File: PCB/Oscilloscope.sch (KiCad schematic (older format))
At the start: 21 parts

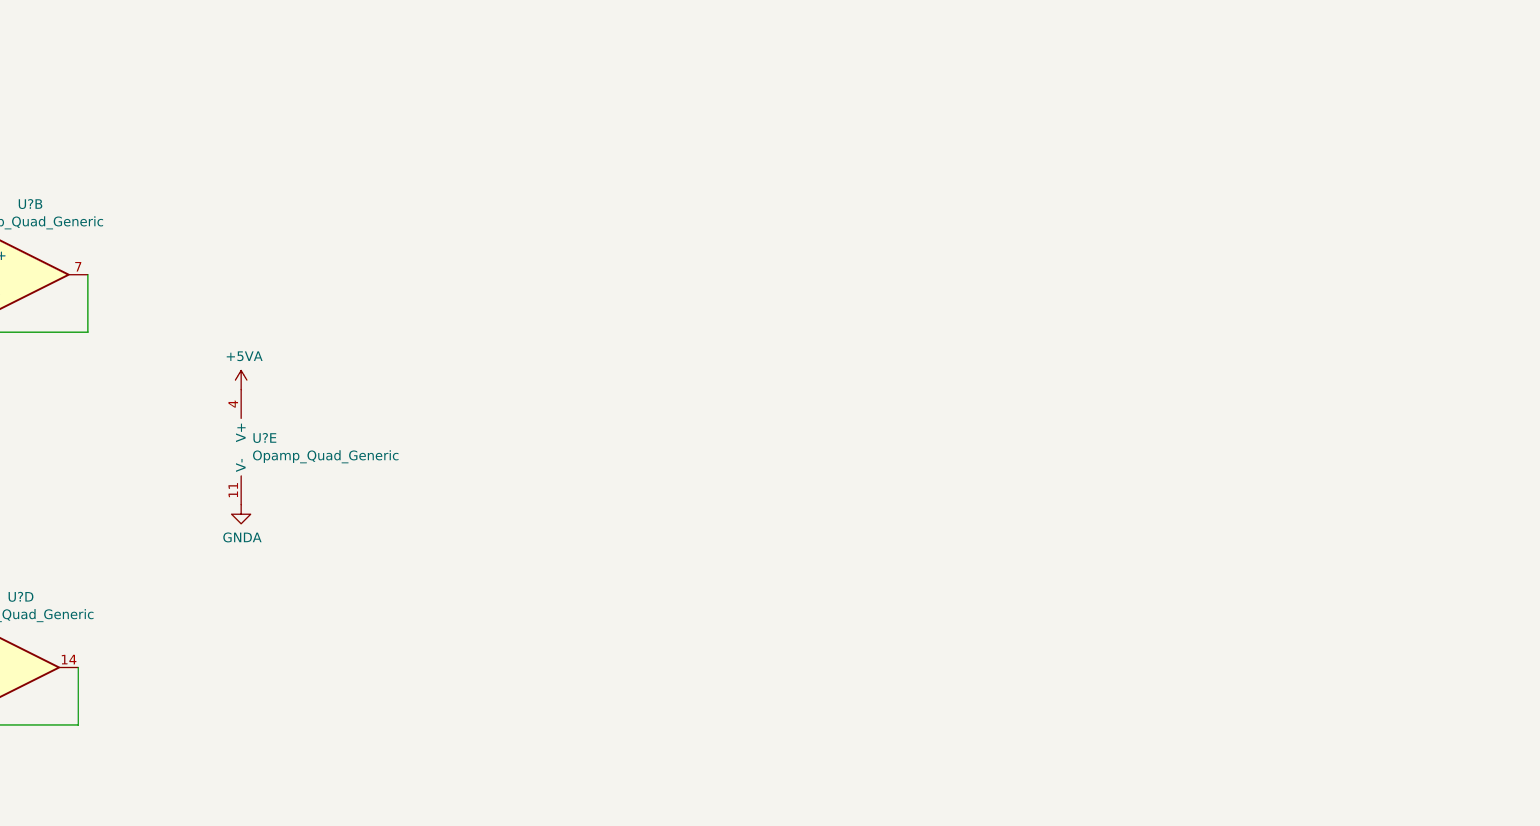
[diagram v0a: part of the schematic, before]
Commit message: Added USB footprint and modified schematic
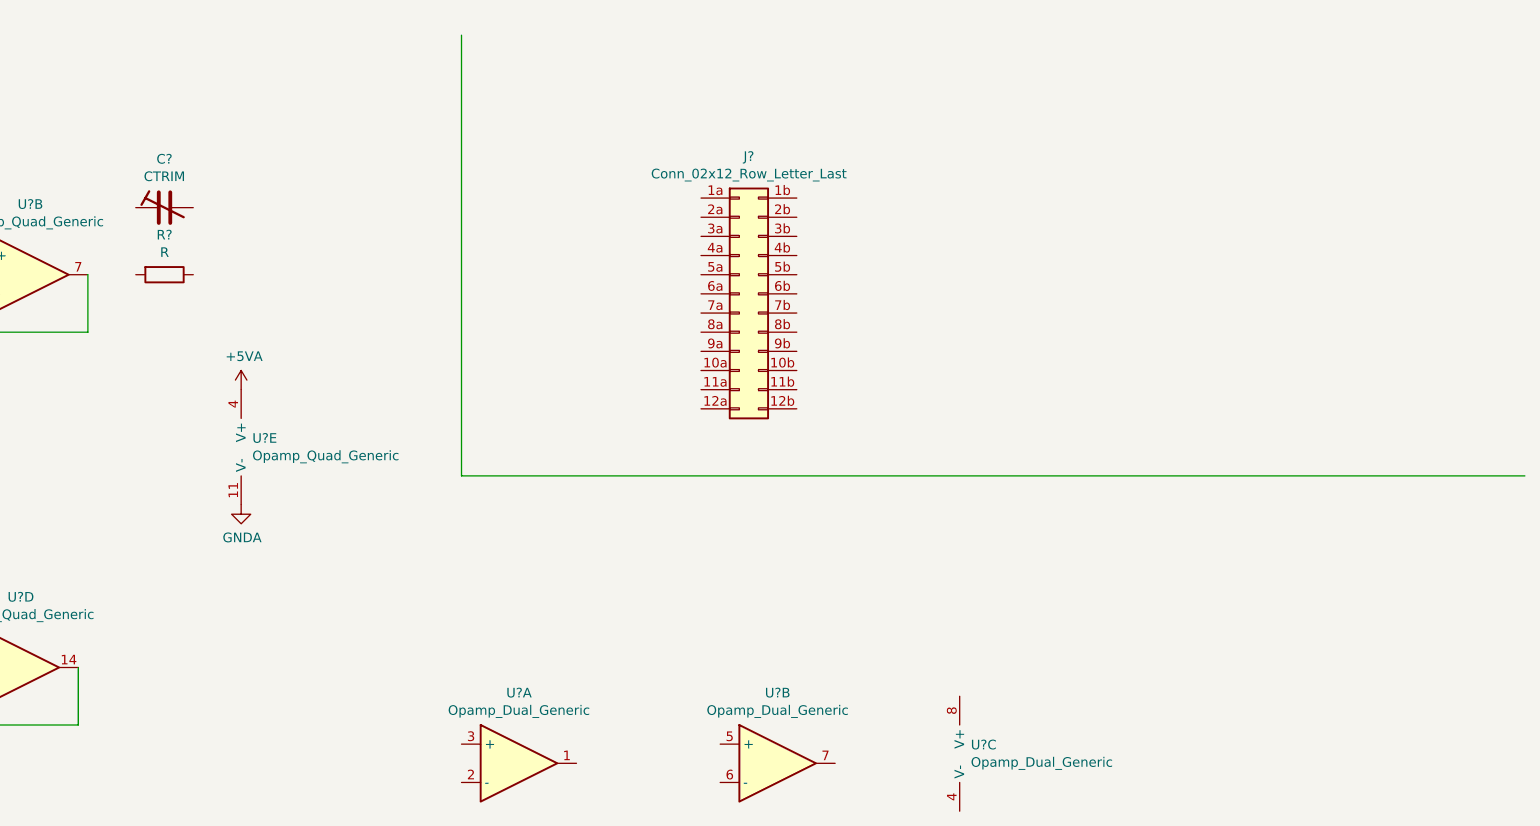
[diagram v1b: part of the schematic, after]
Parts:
- added C?: CTRIM, symbol Device:CTRIM
- added J?: Conn_02x12_Row_Letter_Last, symbol Connector_Generic:Conn_02x12_Row_Letter_Last
- added R?: R, symbol Device:R
- added U? (x3): Opamp_Dual_Generic, symbol Device:Opamp_Dual_Generic
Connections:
- wire segments 44 -> 46
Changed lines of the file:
@@
 $Descr A4 11693 8268
 encoding utf-8
-Sheet 2 5
+Sheet 2 3
 Title ""
 Date ""
@@
 	2850 3900 3000 3900
 $Comp
-L power:GNDA #PWR?
+L power:GNDA #PWR0117
 U 1 1 5E8B3DC5
 P 2550 4050
-F 0 "#PWR?" H 2550 3800 50  0001 C CNN
+F 0 "#PWR0117" H 2550 3800 50  0001 C CNN
 F 1 "GNDA" H 2555 3877 50  0000 C CNN
 F 2 "" H 2550 4050 50  0001 C CNN
@@
 $EndComp
 $Comp
-L power:GNDA #PWR?
+L power:GNDA #PWR0118
 U 1 1 5E8B4AEE
 P 1100 4200
-F 0 "#PWR?" H 1100 3950 50  0001 C CNN
+F 0 "#PWR0118" H 1100 3950 50  0001 C CNN
 F 1 "GNDA" H 1105 4027 50  0000 C CNN
 F 2 "" H 1100 4200 50  0001 C CNN
@@
 $EndComp
 $Comp
-L power:GNDA #PWR?
+L power:GNDA #PWR0119
 U 1 1 5E8B4E02
 P 2850 2150
-F 0 "#PWR?" H 2850 1900 50  0001 C CNN
+F 0 "#PWR0119" H 2850 1900 50  0001 C CNN
 F 1 "GNDA" H 2855 1977 50  0000 C CNN
 F 2 "" H 2850 2150 50  0001 C CNN
@@
 $EndComp
 $Comp
-L power:GNDA #PWR?
+L power:GNDA #PWR0120
 U 1 1 5E8B5E64
 P 850 2000
-F 0 "#PWR?" H 850 1750 50  0001 C CNN
+F 0 "#PWR0120" H 850 1750 50  0001 C CNN
 F 1 "GNDA" H 855 1827 50  0000 C CNN
 F 2 "" H 850 2000 50  0001 C CNN
@@
 	1100 1650 1350 1650
 $Comp
-L power:GNDA #PWR?
+L power:GNDA #PWR0121
 U 1 1 5E8EE81D
 P 2550 2000
-F 0 "#PWR?" H 2550 1750 50  0001 C CNN
+F 0 "#PWR0121" H 2550 1750 50  0001 C CNN
 F 1 "GNDA" H 2555 1827 50  0000 C CNN
 F 2 "" H 2550 2000 50  0001 C CNN
@@
 $EndComp
 $Comp
-L power:GNDA #PWR?
+L power:GNDA #PWR0122
 U 1 1 5E8F1CAA
 P 1100 2150
-F 0 "#PWR?" H 1100 1900 50  0001 C CNN
+F 0 "#PWR0122" H 1100 1900 50  0001 C CNN
 F 1 "GNDA" H 1105 1977 50  0000 C CNN
 F 2 "" H 1100 2150 50  0001 C CNN
@@
 $EndComp
 $Comp
-L power:GNDA #PWR?
+L power:GNDA #PWR0123
 U 1 1 5E8F2DB9
 P 850 4050
-F 0 "#PWR?" H 850 3800 50  0001 C CNN
+F 0 "#PWR0123" H 850 3800 50  0001 C CNN
 F 1 "GNDA" H 855 3877 50  0000 C CNN
 F 2 "" H 850 4050 50  0001 C CNN
@@
 $EndComp
 $Comp
-L power:GNDA #PWR?
+L power:GNDA #PWR0124
 U 1 1 5E8F4144
 P 2850 4200
-F 0 "#PWR?" H 2850 3950 50  0001 C CNN
+F 0 "#PWR0124" H 2850 3950 50  0001 C CNN
 F 1 "GNDA" H 2855 4027 50  0000 C CNN
 F 2 "" H 2850 4200 50  0001 C CNN
@@
 $EndComp
 $Comp
-L power:+5VA #PWR?
+L power:+5VA #PWR0125
 U 1 1 5E907F1D
 P 4500 2350
-F 0 "#PWR?" H 4500 2200 50  0001 C CNN
+F 0 "#PWR0125" H 4500 2200 50  0001 C CNN
 F 1 "+5VA" H 4515 2523 50  0000 C CNN
 F 2 "" H 4500 2350 50  0001 C CNN
@@
 $EndComp
 $Comp
-L power:+5VA #PWR?
+L power:+5VA #PWR0126
 U 1 1 5E9083AD
 P 1100 1300
-F 0 "#PWR?" H 1100 1150 50  0001 C CNN
+F 0 "#PWR0126" H 1100 1150 50  0001 C CNN
 F 1 "+5VA" H 1115 1473 50  0000 C CNN
 F 2 "" H 1100 1300 50  0001 C CNN
@@
 $EndComp
 $Comp
-L power:+5VA #PWR?
+L power:+5VA #PWR0127
 U 1 1 5E90B4C3
 P 2800 1300
-F 0 "#PWR?" H 2800 1150 50  0001 C CNN
+F 0 "#PWR0127" H 2800 1150 50  0001 C CNN
 F 1 "+5VA" H 2815 1473 50  0000 C CNN
 F 2 "" H 2800 1300 50  0001 C CNN
@@
 $EndComp
 $Comp
-L power:+5VA #PWR?
+L power:+5VA #PWR0128
 U 1 1 5E90BBBE
 P 1100 3350
-F 0 "#PWR?" H 1100 3200 50  0001 C CNN
+F 0 "#PWR0128" H 1100 3200 50  0001 C CNN
 F 1 "+5VA" H 1115 3523 50  0000 C CNN
 F 2 "" H 1100 3350 50  0001 C CNN
@@
 $EndComp
 $Comp
-L power:+5VA #PWR?
+L power:+5VA #PWR0129
 U 1 1 5E90CE52
 P 2800 3350
-F 0 "#PWR?" H 2800 3200 50  0001 C CNN
+F 0 "#PWR0129" H 2800 3200 50  0001 C CNN
 F 1 "+5VA" H 2815 3523 50  0000 C CNN
 F 2 "" H 2800 3350 50  0001 C CNN
@@
 $EndComp
 $Comp
-L power:GNDA #PWR?
+L power:GNDA #PWR0130
 U 1 1 5E90F47D
 P 4500 2950
-F 0 "#PWR?" H 4500 2700 50  0001 C CNN
+F 0 "#PWR0130" H 4500 2700 50  0001 C CNN
 F 1 "GNDA" H 4505 2777 50  0000 C CNN
 F 2 "" H 4500 2950 50  0001 C CNN
@@
 Text GLabel 2550 3250 1    50   Input ~ 0
 analog_input_1
+$Comp
+L Connector_Generic:Conn_02x12_Row_Letter_Last J?
+U 1 1 5E8BD1E2
+P 7100 1850
+F 0 "J?" H 7150 2567 50  0000 C CNN
+F 1 "Conn_02x12_Row_Letter_Last" H 7150 2476 50  0000 C CNN
+F 2 "" H 7100 1850 50  0001 C CNN
+F 3 "~" H 7100 1850 50  0001 C CNN
+	1    7100 1850
+	1    0    0    -1
+$EndComp
+$Comp
+L Device:Opamp_Dual_Generic U?
+U 1 1 5E8C2412
+P 5950 4300
+AR Path="/5E84F5D5/5E8C2412" Ref="U?"  Part="1"
+AR Path="/5E84F4C6/5E8C2412" Ref="U?"  Part="1"
+F 0 "U?" H 5950 4667 50  0000 C CNN
+F 1 "Opamp_Dual_Generic" H 5950 4576 50  0000 C CNN
+F 2 "" H 5950 4300 50  0001 C CNN
+F 3 "~" H 5950 4300 50  0001 C CNN
+	1    5950 4300
+	1    0    0    -1
+$EndComp
+$Comp
+L Device:Opamp_Dual_Generic U?
+U 2 1 5E8C2418
+P 7300 4300
+AR Path="/5E84F5D5/5E8C2418" Ref="U?"  Part="2"
+AR Path="/5E84F4C6/5E8C2418" Ref="U?"  Part="2"
+F 0 "U?" H 7300 4667 50  0000 C CNN
+F 1 "Opamp_Dual_Generic" H 7300 4576 50  0000 C CNN
+F 2 "" H 7300 4300 50  0001 C CNN
+F 3 "~" H 7300 4300 50  0001 C CNN
+	2    7300 4300
+	1    0    0    -1
+$EndComp
+$Comp
+L Device:Opamp_Dual_Generic U?
+U 3 1 5E8C241E
+P 8350 4250
+AR Path="/5E84F5D5/5E8C241E" Ref="U?"  Part="3"
+AR Path="/5E84F4C6/5E8C241E" Ref="U?"  Part="3"
+F 0 "U?" H 8308 4296 50  0000 L CNN
+F 1 "Opamp_Dual_Generic" H 8308 4205 50  0000 L CNN
+F 2 "" H 8350 4250 50  0001 C CNN
+F 3 "~" H 8350 4250 50  0001 C CNN
+	3    8350 4250
+	1    0    0    -1
+$EndComp
+$Comp
+L Device:R R?
+U 1 1 5E90D0F4
+P 4100 1750
+F 0 "R?" V 3893 1750 50  0000 C CNN
+F 1 "R" V 3984 1750 50  0000 C CNN
+F 2 "" V 4030 1750 50  0001 C CNN
+F 3 "~" H 4100 1750 50  0001 C CNN
+	1    4100 1750
+	0    1    1    0
+$EndComp
+$Comp
+L Device:CTRIM C?
+U 1 1 5E90E27B
+P 4100 1400
+F 0 "C?" V 4353 1400 50  0000 C CNN
+F 1 "CTRIM" V 4262 1400 50  0000 C CNN
+F 2 "" H 4100 1400 50  0001 C CNN
+F 3 "~" H 4100 1400 50  0001 C CNN
+	1    4100 1400
+	0    -1   -1   0
+$EndComp
+Wire Wire Line
+	11200 2800 5650 2800
+Wire Wire Line
+	5650 2800 5650 500
 $EndSCHEMATC

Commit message: Advancing in the schmatic. Power to be finished
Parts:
- removed C?: CTRIM, symbol Device:CTRIM
- removed R?: R, symbol Device:R
- added D? (x4): D_Zener, symbol Device:D_Zener
- added R? (x9): R, symbol Device:R
- added R? (x23): 100R, symbol Device:R
- added U? (x5): LM2901, symbol Comparator:LM2901
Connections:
- net labels added: analog_output_1, analog_output_2, analon_input_1, analon_input_2, analon_input_3, analon_input_4, digital_input_1, digital_input_10, digital_input_11, digital_input_12, digital_input_13, digital_input_14, digital_input_15, digital_input_16, digital_input_17, digital_input_18, digital_input_19, digital_input_2, digital_input_20, digital_input_21, digital_input_22, digital_input_23, digital_input_24, digital_input_3, digital_input_4, digital_input_5, digital_input_6, digital_input_7, digital_input_8, digital_input_9, trigger_1, trigger_2, trigger_3, trigger_4
- net labels removed: analog_input_1
- wire segments 46 -> 74
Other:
- moved on the sheet: J?, R?, U?A, U?B, U?C, U?D, U?E

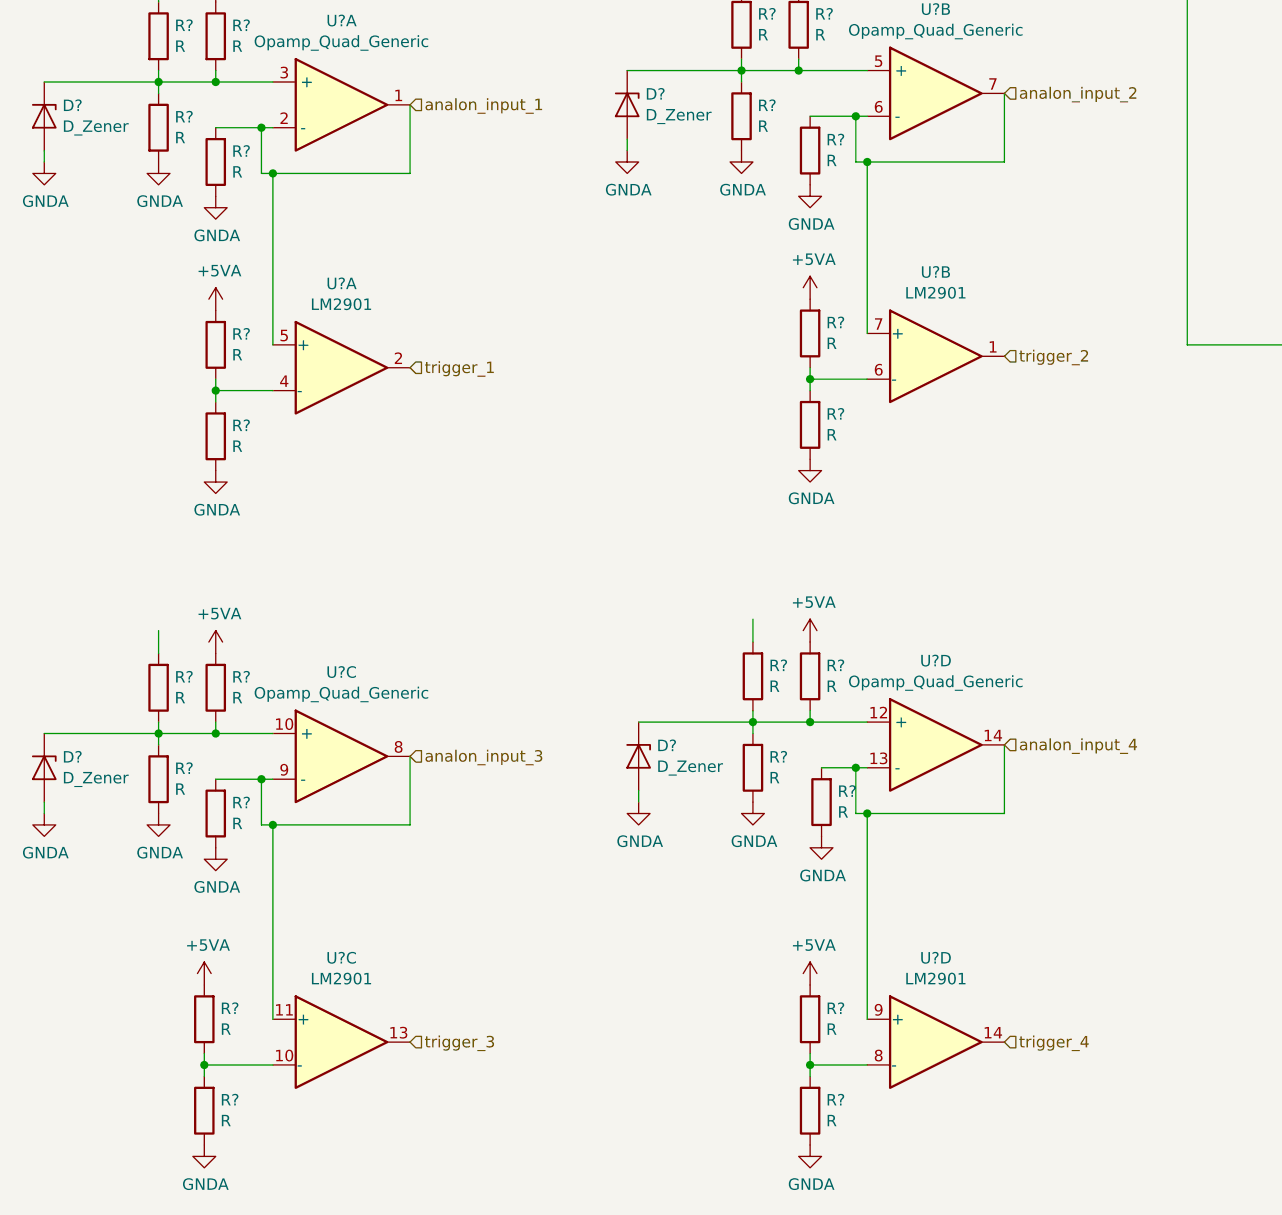
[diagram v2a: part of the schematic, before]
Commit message: Changed microcontroller, schemtic modified
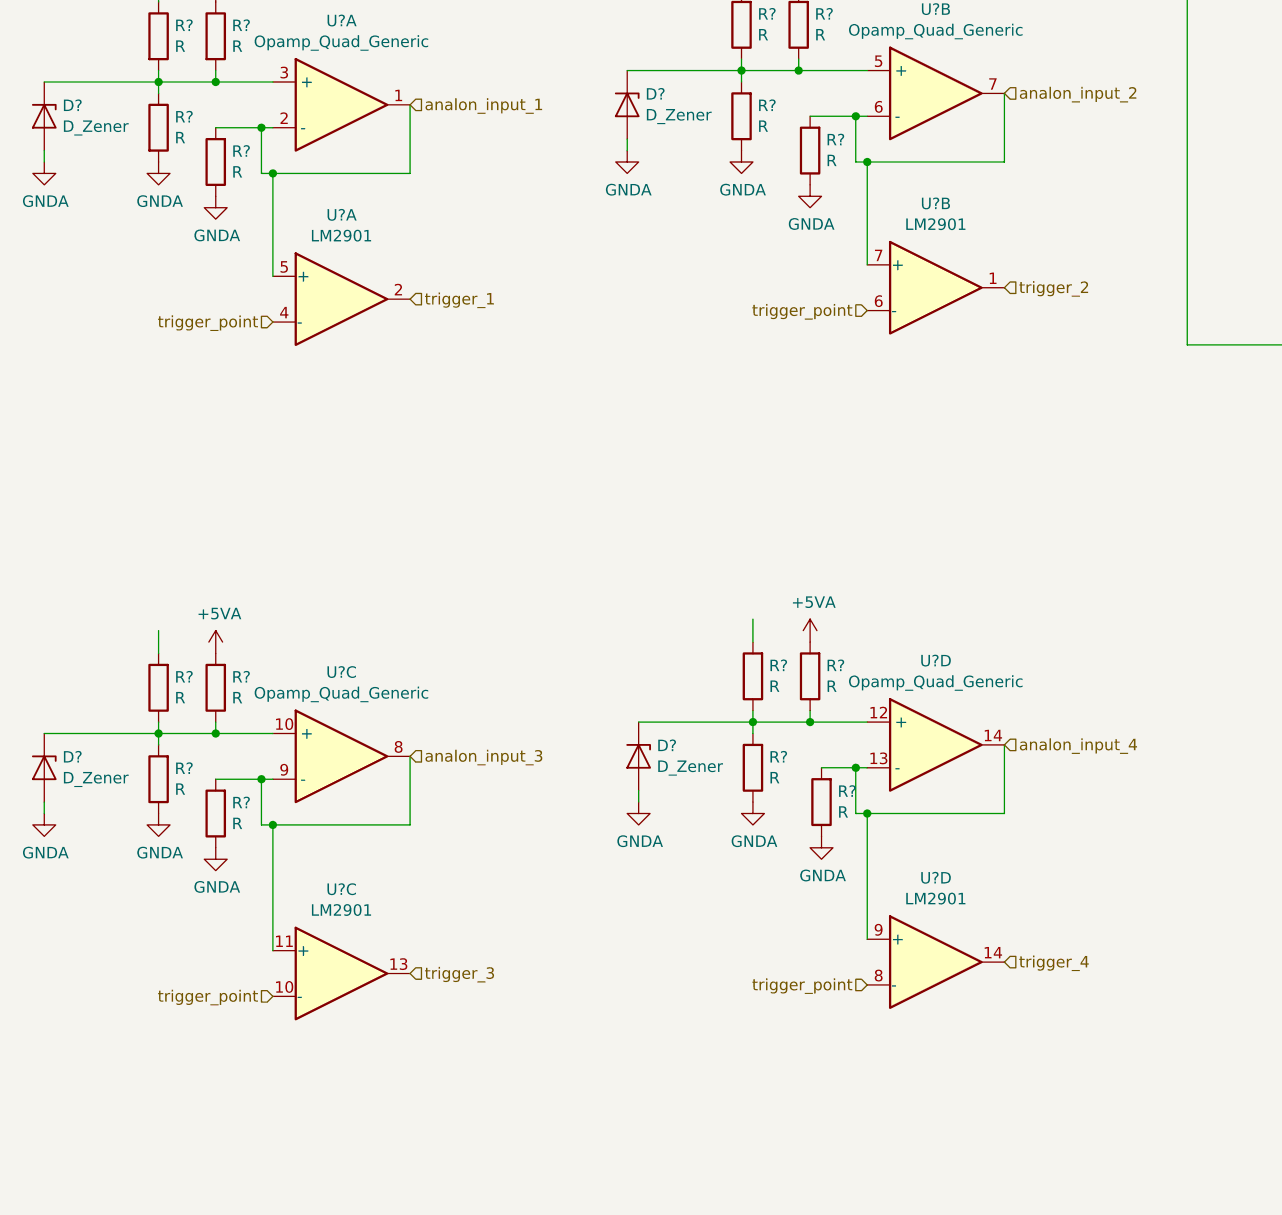
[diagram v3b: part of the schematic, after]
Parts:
- removed R? (x8): R, symbol Device:R
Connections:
- net labels added: trigger_point
- wire segments 74 -> 62
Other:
- moved on the sheet: U?A, U?B, U?C, U?D

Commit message: Advancement in schematic regarding oscilloscope and power supply
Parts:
- added FB? (x2): Ferrite_Bead, symbol Device:Ferrite_Bead
- added R? (x2): 27k, symbol Device:R
- added R? (x2): 10k, symbol Device:R
- added R? (x4): R, symbol Device:R
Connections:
- net labels added: +15V, -15V
- wire segments 62 -> 102
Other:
- note added: "Channel 1"
- note added: "Channel 1\n"
- note added: "Channel 2"
- note added: "Channel 2\n"
- note added: "Channel 3\n"
- note added: "Channel 4"
- note added: "DAC\n"
- note added: "Filtering between analog and digital voltage domain"
- note added: "Logic analyzer\n"
- note added: "Oscilloscope"
- note added: "Used with 15V, scale and amplify 1.65-3.3 ->15"
- moved on the sheet: D?, R?, U?A, U?B, U?C, U?D, U?E
